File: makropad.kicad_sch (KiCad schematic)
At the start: 27 parts, among them J1 OLED_DISPLAY, SW1 SW_Push_45deg, SW10 SW_Push_45deg, SW11 RotaryEncoder_Switch, SW12 RotaryEncoder_Switch, SW2 SW_Push_45deg, SW3 SW_Push_45deg, SW4 SW_Push_45deg, SW5 SW_Push_45deg, SW6 SW_Push_45deg, SW7 SW_Push_45deg, SW8 SW_Push_45deg, SW9 SW_Push_45deg, U1 PCF8574A, U2 MOUDLE-SEEEDUINO-XIAO

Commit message: Finish pcb
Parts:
- added R1, R2, R3, R4, R5, R6: 10k, Resistor_SMD:R_1206_3216Metric, symbol Device:R
- D1, D10, D11, D12, D2, D3, D4, D5, D6, D7, D8, D9: footprint Diode_THT:D_DO-35_SOD27_P7.62mm_Horizontal -> Diode_SMD:D_1206_3216Metric
- J1: footprint Connector_PinHeader_2.54mm:PinHeader_1x04_P2.54mm_Vertical -> Components:SSD1306-0.91-OLED-4pin-128x32
- SW1, SW10, SW2, SW3, SW4, SW5, SW6, SW7, SW8, SW9: footprint MX_Solderable:MX-Solderable-1U -> Components:MX-Solderable-1U
- U1: footprint (none) -> Components:SOIC127P1032X265-16N
- U2: footprint (none) -> Components:XIAO-Generic-Hybrid-14P-2.54-21X17.8MM
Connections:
- net ENC_1_A: now also R6.1
- net ENC_1_B: now also R5.1
- net ENC_2_A: now also R4.1
- net ENC_2_B: now also R3.1
- net I2C_SCL: now also R2.1
- net I2C_SDA: now also R1.1
- net VCC: now also R1.2, R2.2, R3.2, R4.2, R5.2, R6.2
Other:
- note added: "Encoders"
- note added: "I/O Expander (for encoders)"
- note added: "OLED"
- note added: "Pull Up Resistors"
- note added: "RP2040"
- note added: "Switch Grid"
- moved on the sheet: SW11, SW12, U1, U2

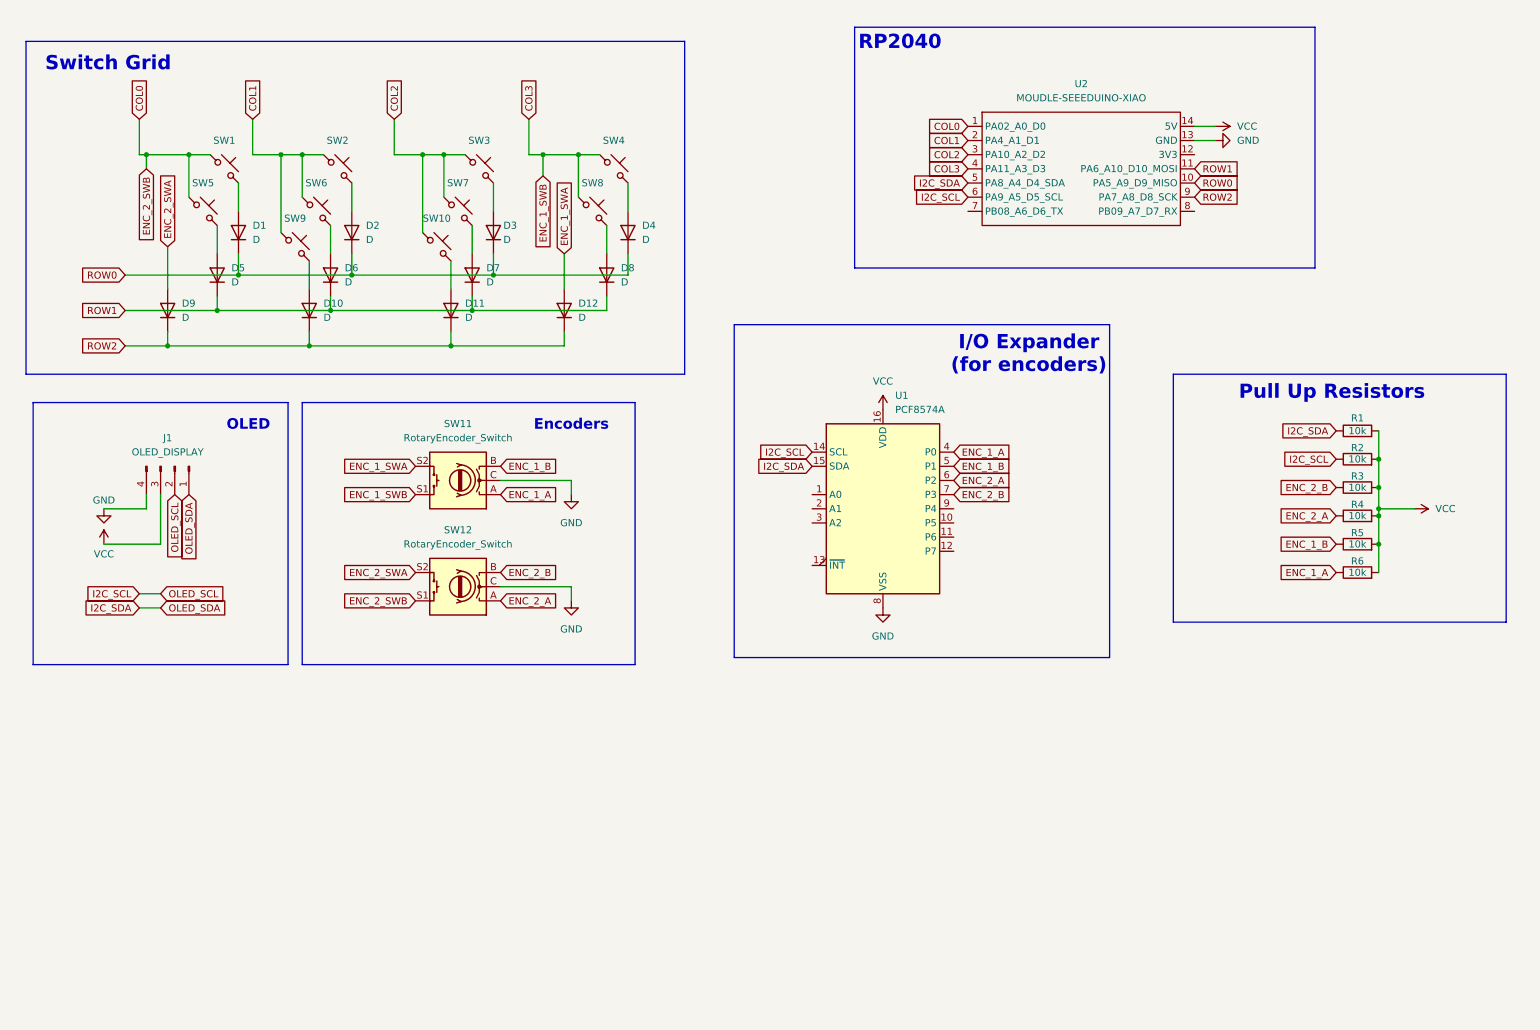
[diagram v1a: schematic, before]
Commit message: feat: finish pcb placement
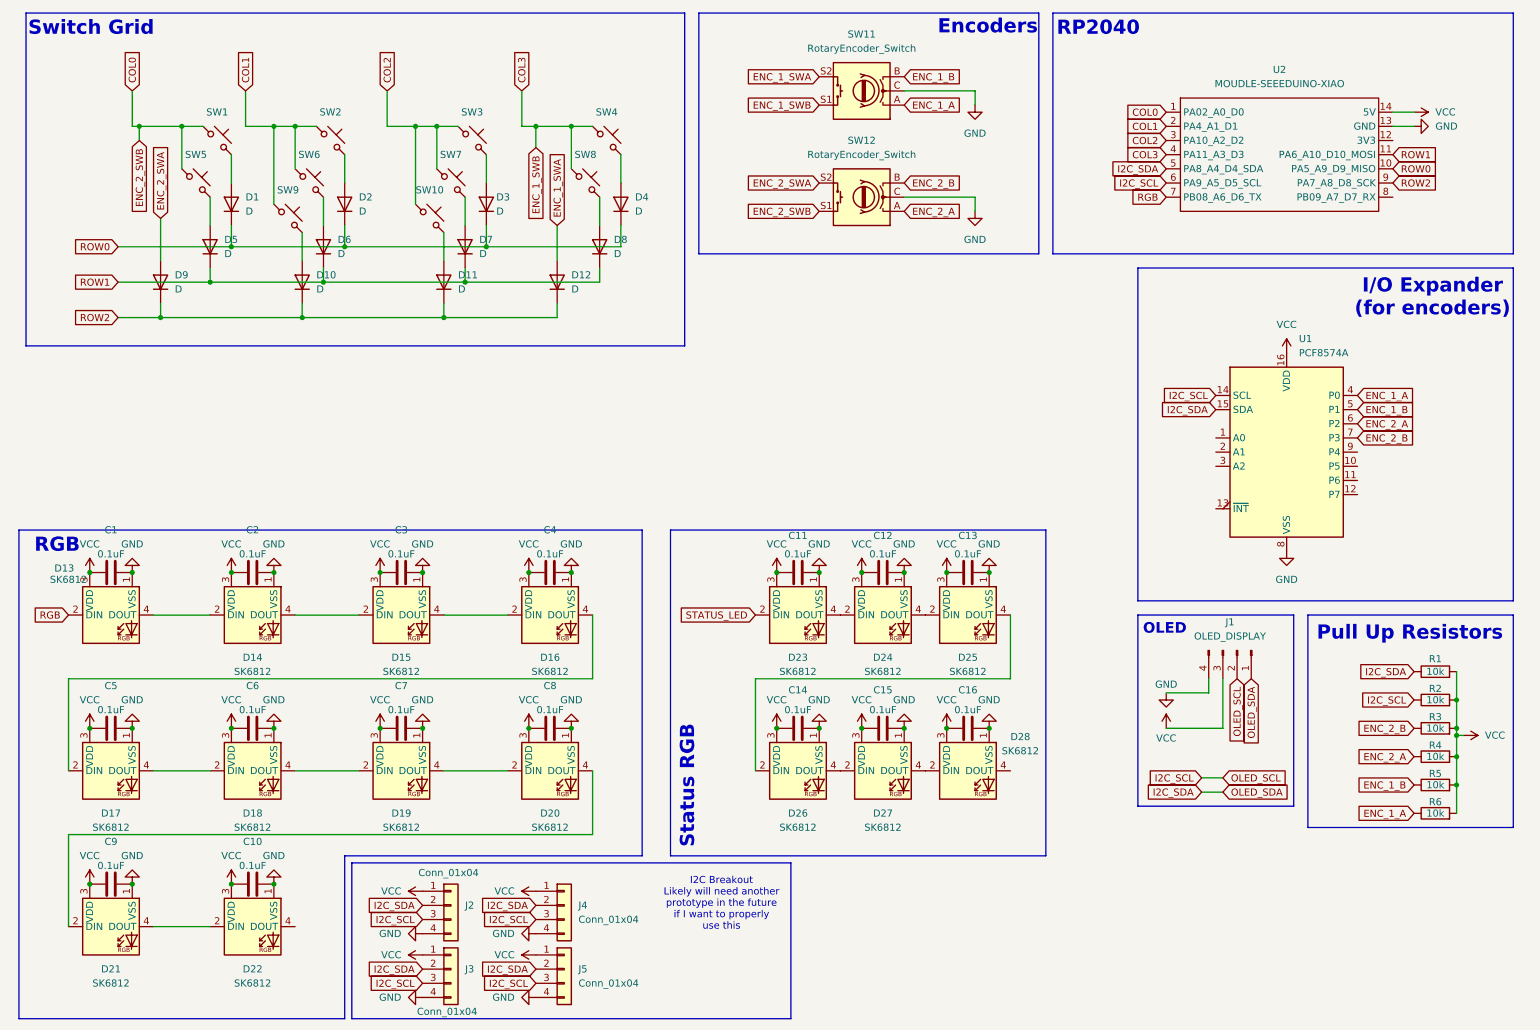
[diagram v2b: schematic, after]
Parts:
- added C1, C10, C11, C12, C13, C14, C15, C16, C2, C3, C4, C5, C6, C7, C8, C9: 0.1uF, symbol Device:C
- added D13, D14, D15, D16, D17, D18, D19, D20, D21, D22: SK6812, Components:SK6812MINI-E, symbol SK6812_CUSTOM:SK6812_Custom
- added D23, D24, D25, D26, D27, D28: SK6812, LED_SMD:LED_SK6812_PLCC4_5.0x5.0mm_P3.2mm, symbol SK6812_CUSTOM:SK6812_Custom
- added J2, J3, J4, J5: Conn_01x04, Connector_PinSocket_2.54mm:PinSocket_1x04_P2.54mm_Vertical, symbol Connector_Generic:Conn_01x04
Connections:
- net GND: now also C1.2, C10.2, C11.2, C12.2, C13.2, C14.2, C15.2, C16.2, C2.2, C3.2, C4.2, C5.2, C6.2, C7.2, C8.2, C9.2, D13.1 (VSS), D14.1 (VSS), D15.1 (VSS), D16.1 (VSS), D17.1 (VSS), D18.1 (VSS), D19.1 (VSS), D20.1 (VSS), D21.1 (VSS), D22.1 (VSS), D23.1 (VSS), D24.1 (VSS), D25.1 (VSS), D26.1 (VSS), D27.1 (VSS), D28.1 (VSS), J2.4 (Pin_4), J3.4 (Pin_4), J4.4 (Pin_4), J5.4 (Pin_4)
- net I2C_SCL: now also J2.3 (Pin_3), J3.3 (Pin_3), J4.3 (Pin_3), J5.3 (Pin_3)
- net I2C_SDA: now also J2.2 (Pin_2), J3.2 (Pin_2), J4.2 (Pin_2), J5.2 (Pin_2)
- net VCC: now also C1.1, C10.1, C11.1, C12.1, C13.1, C14.1, C15.1, C16.1, C2.1, C3.1, C4.1, C5.1, C6.1, C7.1, C8.1, C9.1, D13.3 (VDD), D14.3 (VDD), D15.3 (VDD), D16.3 (VDD), D17.3 (VDD), D18.3 (VDD), D19.3 (VDD), D20.3 (VDD), D21.3 (VDD), D22.3 (VDD), D23.3 (VDD), D24.3 (VDD), D25.3 (VDD), D26.3 (VDD), D27.3 (VDD), D28.3 (VDD), J2.1 (Pin_1), J3.1 (Pin_1), J4.1 (Pin_1), J5.1 (Pin_1)
- net RGB: now reaches U2.7 (PB08_A6_D6_TX)
- net RGB: now also D13.2 (DIN)
- new net: D27.4 (DOUT), D28.2 (DIN)
- new net: D13.4 (DOUT), D14.2 (DIN)
- new net: D14.4 (DOUT), D15.2 (DIN)
- new net: D17.4 (DOUT), D18.2 (DIN)
- new net: D18.4 (DOUT), D19.2 (DIN)
- new net: D20.4 (DOUT), D21.2 (DIN)
- new net: D21.4 (DOUT), D22.2 (DIN)
- new net: D26.4 (DOUT), D27.2 (DIN)
- new net: D19.4 (DOUT), D20.2 (DIN)
- new net: D25.4 (DOUT), D26.2 (DIN)
- new net: D15.4 (DOUT), D16.2 (DIN)
- new net: D16.4 (DOUT), D17.2 (DIN)
- new net: D24.4 (DOUT), D25.2 (DIN)
- new net: D23.4 (DOUT), D24.2 (DIN)
- new net STATUS_LED: D23.2 (DIN)
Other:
- note added: "I2C Breakout Likely will need another prototype in the future if I want to properly use this"
- note added: "RGB"
- note added: "Status RGB"
- moved on the sheet: D1, D10, D11, D12, D2, D3, D4, D5, D6, D7, D8, D9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

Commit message: feat: fully route pcb
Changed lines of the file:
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@@
 	(polyline
 		(pts
-			(xy 15.24 106.68) (xy 127 106.68)
+			(xy 15.24 105.41) (xy 127 105.41)
 		)
 		(stroke
@@
 	(polyline
 		(pts
-			(xy 15.24 106.68) (xy 15.24 194.31)
+			(xy 15.24 105.41) (xy 15.24 194.31)
 		)
 		(stroke
@@
 	(polyline
 		(pts
-			(xy 127 165.1) (xy 127 106.68)
+			(xy 127 165.1) (xy 127 105.41)
 		)
 		(stroke
@@
 	)
 	(rectangle
-		(start 132.08 106.68)
-		(end 199.39 165.1)
+		(start 132.08 105.41)
+		(end 199.39 163.83)
 		(stroke
 			(width 0)
@@
 	(text "RGB"
 		(exclude_from_sim no)
-		(at 22.098 109.474 0)
+		(at 19.558 108.458 0)
 		(effects
 			(font

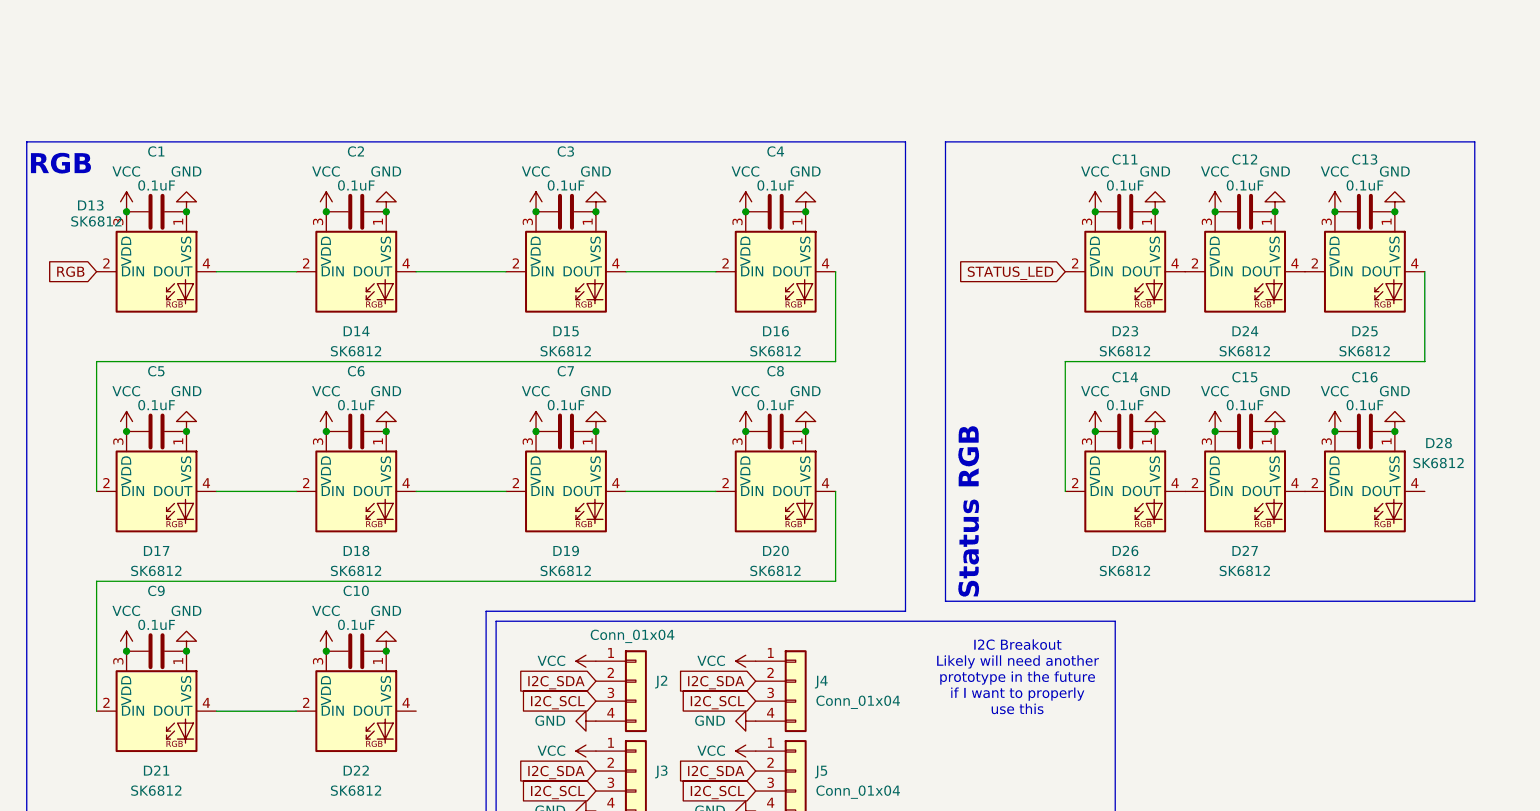
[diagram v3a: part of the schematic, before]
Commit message: feat: add 3d renders
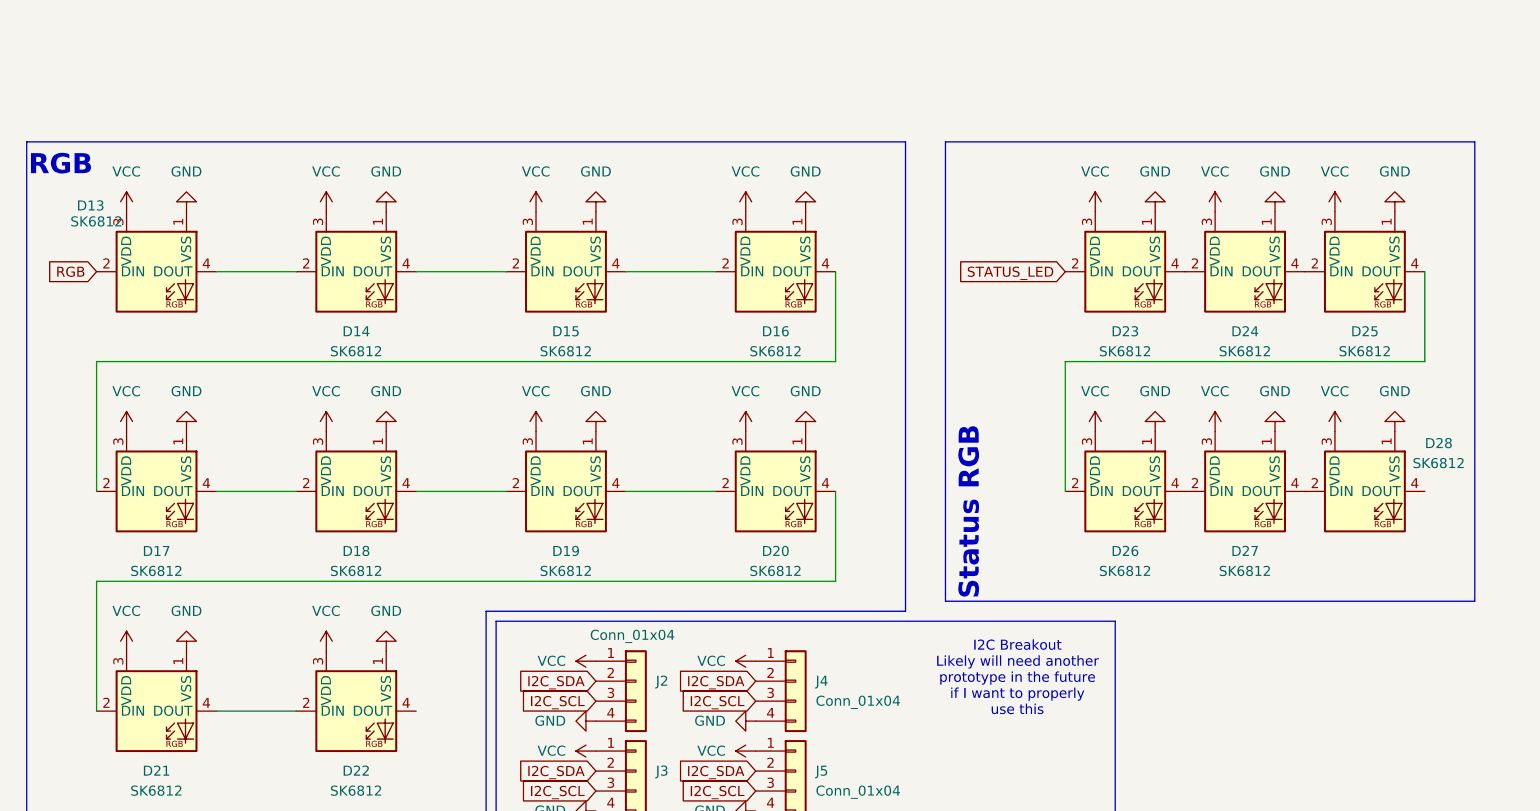
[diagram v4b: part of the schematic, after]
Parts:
- removed C1, C10, C11, C12, C13, C14, C15, C16, C2, C3, C4, C5, C6, C7, C8, C9: 0.1uF, symbol Device:C
- J2, J3, J4, J5: footprint Connector_PinSocket_2.54mm:PinSocket_1x04_P2.54mm_Vertical -> Components:4pin
- SW11, SW12: footprint Rotary_Encoder:RotaryEncoder_Alps_EC11E-Switch_Vertical_H20mm -> Components:encoder
